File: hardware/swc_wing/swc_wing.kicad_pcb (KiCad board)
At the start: 2 copper layers, 62.8 x 58.7 mm, 51 parts, among them J1 Conn_01x06_Female, J2 Conn_01x04, J3 Conn_01x06_Female, J4 Conn_01x01_Female, Q1 2N7002, Q2 2N7002, Q3 2N7002, Q4 2N7002, Q5 2N7002, SW1 SW_Push_LED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

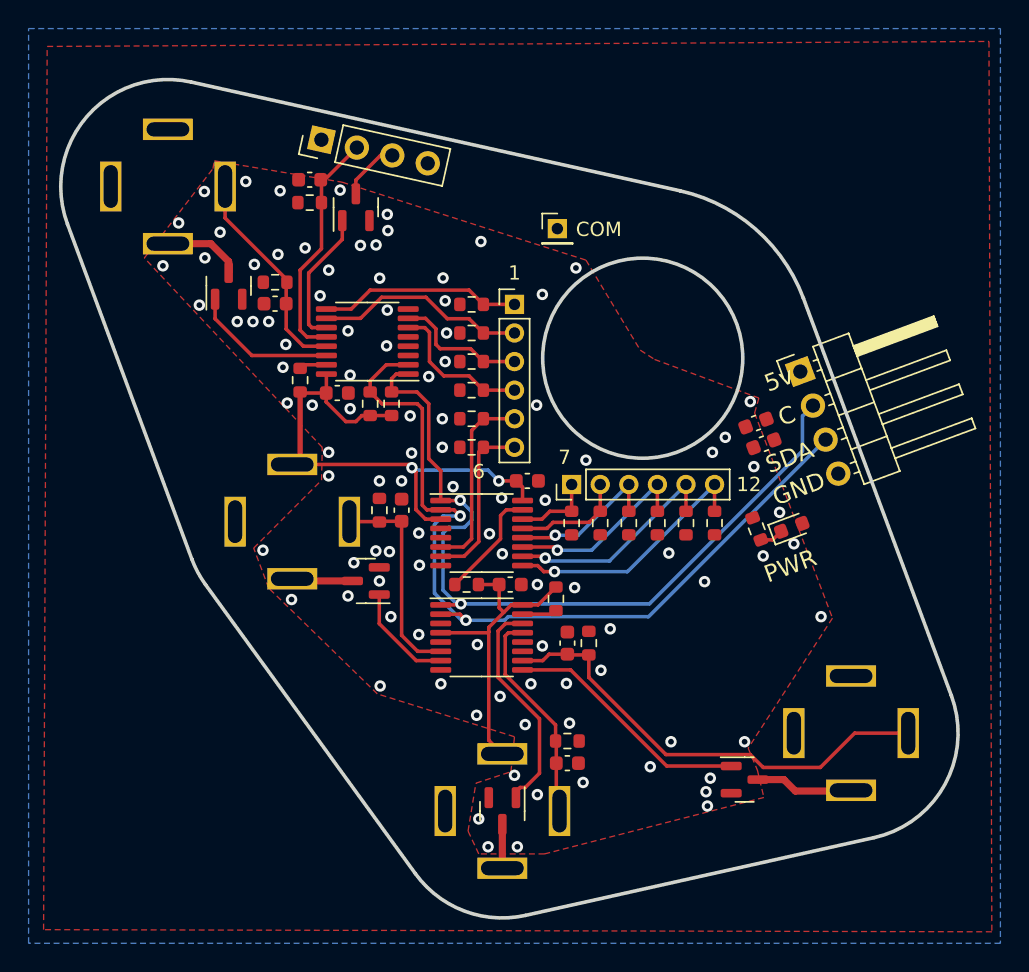
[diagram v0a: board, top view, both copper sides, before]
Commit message: 3.3v-ify wing
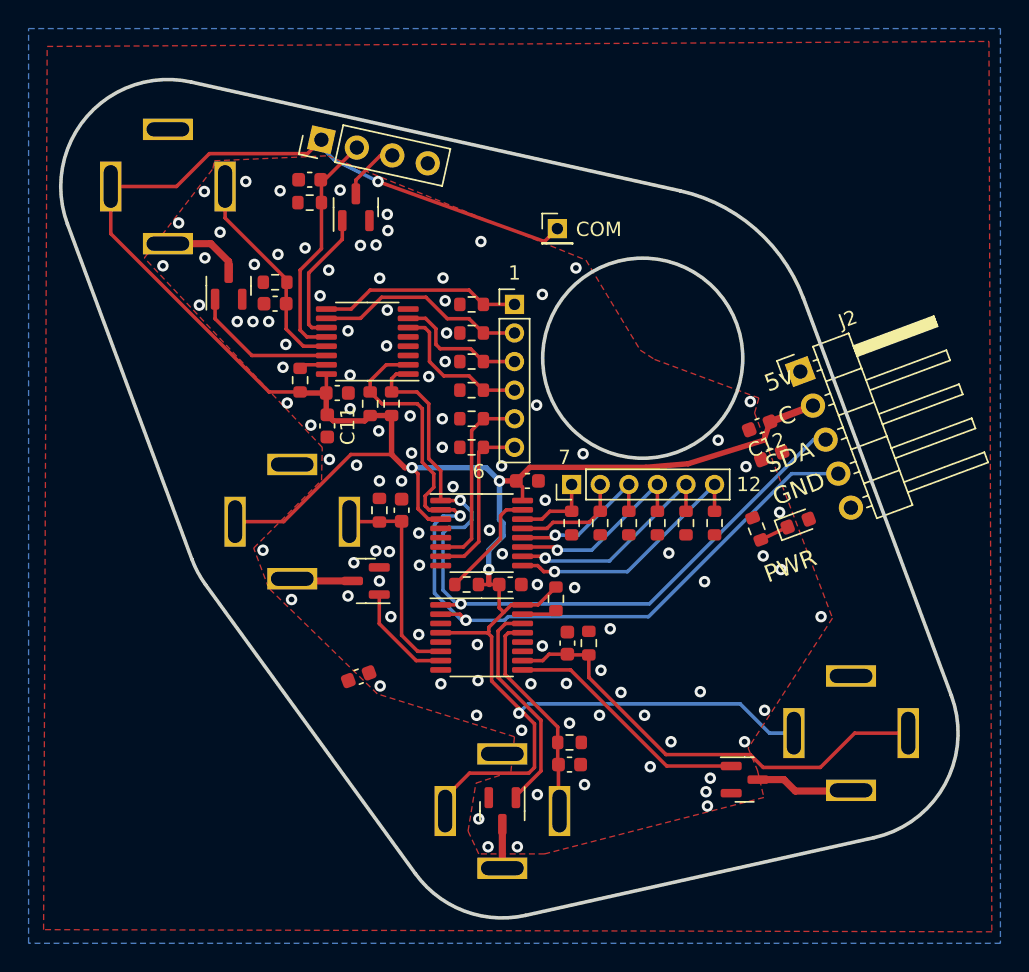
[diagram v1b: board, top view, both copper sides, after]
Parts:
- added C11: 1u, Capacitor_SMD:C_0603_1608Metric, F.Cu at (36.9, 83.8)
- added C12: 1u, Capacitor_SMD:C_0603_1608Metric, F.Cu at (67.2, 83.8)
- J2: value Conn_01x04 -> Conn_01x05; footprint Connector_PinHeader_2.54mm:PinHeader_1x04_P2.54mm_Horizontal -> Connector_PinHeader_2.54mm:PinHeader_1x05_P2.54mm_Horizontal
- moved C10 32.7 mm to (39.1, 101.3), turned to 20.4 degrees
- moved C9 2.55 mm to (68.0, 85.9)
- moved D1 0.54 mm to (69.8, 90.6)
- moved R4 0.18 mm to (53.9, 106.0)
- moved C4 0.18 mm to (53.9, 107.5)
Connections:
- C6 pad 1: +5V -> +3.3V
- C7 pad 1: +5V -> +3.3V
- C8 pad 1: +5V -> +3.3V
- J2 pad 2: SCL -> +3.3V
- J2 pad 3: SDA -> SCL
- J2 pad 4: GND -> SDA
- J4 pad 1: +5V -> +3.3V
- R10 pad 1: +5V -> +3.3V
- R6 pad 2: +5V -> +3.3V
- R7 pad 2: +5V -> +3.3V
- R8 pad 2: +5V -> +3.3V
- R9 pad 1: +5V -> +3.3V
- SW1 pad 1: +5V -> +3.3V
- SW2 pad 1: +5V -> +3.3V
- SW3 pad 1: +5V -> +3.3V
- SW4 pad 1: +5V -> +3.3V
- SW5 pad 1: +5V -> +3.3V
- U1 pad 16: +5V -> +3.3V
- U2 pad 16: +5V -> +3.3V
- U2 pad 3: +5V -> +3.3V
- U3 pad 16: +5V -> +3.3V
- U3 pad 4: +5V -> +3.3V
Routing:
- net +3.3V: track 0.00 -> 180.4 mm, vias 0 -> 5
- net +5V: track 59.2 -> 0.00 mm, vias 2 -> 0
- net SCL: track 56.7 -> 55.1 mm
- net GND: vias 101 -> 105

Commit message: wing tweaks
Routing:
- net GND: vias 105 -> 106
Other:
- board text added: "3v"
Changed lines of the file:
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@@
     (property "Sheetname" "")
     (attr through_hole)
-    (fp_text reference "J2" (at 4.385 -2.27 20.4) (layer "F.SilkS")
+    (fp_text reference "J2" (at 4.385 -2.27 20.4) (layer "F.SilkS") hide
       (effects (font (size 1 1) (thickness 0.15)))
     )
@@
     (property "Sheetname" "")
     (attr smd)
-    (fp_text reference "C11" (at 0 -1.43 90) (layer "F.SilkS")
+    (fp_text reference "C11" (at 0 -1.43 90) (layer "F.SilkS") hide
       (effects (font (size 1 1) (thickness 0.15)))
     )
@@
     (property "Sheetname" "")
     (attr smd)
-    (fp_text reference "C12" (at 0 -1.43 20.4) (layer "F.SilkS")
+    (fp_text reference "C12" (at 0 -1.43 20.4) (layer "F.SilkS") hide
       (effects (font (size 1 1) (thickness 0.15)))
     )
@@
   (gr_arc (start 50.770706 118.050213) (mid 46.48445 117.744753) (end 43.0694 115.136547) (layer "Edge.Cuts") (width 0.25))
   (gr_arc (start 28.380921 94.906654) (mid 27.838485 94.041203) (end 27.418667 93.110077) (layer "Edge.Cuts") (width 0.25))
-  (gr_text "SCL" (at 68.1 83.5 20.4) (layer "B.SilkS")
+  (gr_text "SCL" (at 68.9 85.9 20.4) (layer "B.SilkS")
     (effects (font (size 1.2 1.2) (thickness 0.15)) (justify mirror))
   )
@@
     (effects (font (size 1 1) (thickness 0.15)) (justify mirror))
   )
+  (gr_text "3v" (at 68.6 83.3 20.4) (layer "B.SilkS")
+    (effects (font (size 1.2 1.2) (thickness 0.15)) (justify mirror))
+  )
   (gr_text "7" (at 52.5 88) (layer "B.SilkS")
     (effects (font (size 1 1) (thickness 0.15)) (justify mirror))
@@
     (effects (font (size 1 1) (thickness 0.15)) (justify mirror))
   )
-  (gr_text "GND" (at 69.65 88.3 20.4) (layer "B.SilkS")
+  (gr_text "GND" (at 70.75 90.65 20.4) (layer "B.SilkS")
     (effects (font (size 1.2 1.2) (thickness 0.15)) (justify mirror))
   )
@@
     (effects (font (size 1.2 1.2) (thickness 0.15)) (justify mirror))
   )
-  (gr_text "SDA" (at 68.95 85.95 20.4) (layer "B.SilkS")
+  (gr_text "SDA" (at 69.75 88.25 20.4) (layer "B.SilkS")
     (effects (font (size 1.2 1.2) (thickness 0.15)) (justify mirror))
   )
@@
     (effects (font (size 1 1) (thickness 0.15)) (justify mirror))
   )
-  (gr_text "SDA" (at 69.25 86 20.4) (layer "F.SilkS")
+  (gr_text "SDA" (at 70.05 88.2 20.4) (layer "F.SilkS")
     (effects (font (size 1.2 1.2) (thickness 0.15)))
   )
@@
     (effects (font (size 1 1) (thickness 0.15)))
   )
-  (gr_text "GND" (at 69.9 88.2 20.4) (layer "F.SilkS")
+  (gr_text "GND" (at 72.75 91.8 20.4) (layer "F.SilkS")
     (effects (font (size 1.2 1.2) (thickness 0.15)))
   )
@@
     (effects (font (size 1 1) (thickness 0.15)))
   )
-  (gr_text "C" (at 69.05 83.1 20.4) (layer "F.SilkS")
+  (gr_text "C" (at 70.15 85.45 20.4) (layer "F.SilkS")
     (effects (font (size 1.2 1.2) (thickness 0.15)))
   )
-  (gr_text "PWR" (at 69.3 93.6 20.4) (layer "F.SilkS")
+  (gr_text "PWR" (at 68.8 93.7 20.4) (layer "F.SilkS")
     (effects (font (size 1.2 1.2) (thickness 0.15)))
   )
   (gr_text "7" (at 53.5 86) (layer "F.SilkS")
     (effects (font (size 1 1) (thickness 0.15)))
+  )
+  (gr_text "3v" (at 69.1 83.15 20.4) (layer "F.SilkS")
+    (effects (font (size 1.2 1.2) (thickness 0.15)))
   )
   (segment (start 36.494867 66.627287) (end 36.444867 66.577287) (width 0.25) (layer "F.Cu") (net 1))
@@
   (via (at 25.4 72.6) (size 0.8) (drill 0.4) (layers "F.Cu" "B.Cu") (net 2))
   (via (at 68.55 89.85) (size 0.8) (drill 0.4) (layers "F.Cu" "B.Cu") (net 2))
-  (via (at 56.7 98) (size 0.8) (drill 0.4) (layers "F.Cu" "B.Cu") (net 2))
+  (via (at 56.7 97.6) (size 0.8) (drill 0.4) (layers "F.Cu" "B.Cu") (net 2))
   (via (at 45.15 79.3) (size 0.8) (drill 0.4) (layers "F.Cu" "B.Cu") (net 2))
   (via (at 38.763148 93.374802) (size 0.8) (drill 0.4) (layers "F.Cu" "B.Cu") (net 2))
@@
   (via (at 39.220903 71.171965) (size 0.8) (drill 0.4) (layers "F.Cu" "B.Cu") (net 2))
   (via (at 33.8 79.7) (size 0.8) (drill 0.4) (layers "F.Cu" "B.Cu") (net 2))
-  (via (at 54.207826 95.114496) (size 0.8) (drill 0.4) (layers "F.Cu" "B.Cu") (net 2))
+  (via (at 54.25 95.2) (size 0.8) (drill 0.4) (layers "F.Cu" "B.Cu") (net 2))
   (via (at 54.9 108.9) (size 0.8) (drill 0.4) (layers "F.Cu" "B.Cu") (net 2))
   (via (at 47.35 104.05) (size 0.8) (drill 0.4) (layers "F.Cu" "B.Cu") (net 2))
@@
   (via (at 52.15 89) (size 0.8) (drill 0.4) (layers "F.Cu" "B.Cu") (net 2))
   (via (at 43.3 98.4) (size 0.8) (drill 0.4) (layers "F.Cu" "B.Cu") (net 2))
-  (via (at 63.3 94.7) (size 0.8) (drill 0.4) (layers "F.Cu" "B.Cu") (net 2))
+  (via (at 63.85 93.75) (size 0.8) (drill 0.4) (layers "F.Cu" "B.Cu") (net 2))
   (via (at 36.4 74.7) (size 0.8) (drill 0.4) (layers "F.Cu" "B.Cu") (net 2))
   (via (at 41.05 78.2) (size 0.8) (drill 0.4) (layers "F.Cu" "B.Cu") (net 2))
@@
   (via (at 42.7 83.1) (size 0.8) (drill 0.4) (layers "F.Cu" "B.Cu") (net 2))
   (via (at 51.6 94.9) (size 0.8) (drill 0.4) (layers "F.Cu" "B.Cu") (net 2))
-  (via (at 60.8 92.7) (size 0.8) (drill 0.4) (layers "F.Cu" "B.Cu") (net 2))
+  (via (at 61.5 92.7) (size 0.8) (drill 0.4) (layers "F.Cu" "B.Cu") (net 2))
   (via (at 41.140943 70.132385) (size 0.8) (drill 0.4) (layers "F.Cu" "B.Cu") (net 2))
   (via (at 45.25 77.3) (size 0.8) (drill 0.4) (layers "F.Cu" "B.Cu") (net 2))
@@
   (via (at 41.35 97.15) (size 0.8) (drill 0.4) (layers "F.Cu" "B.Cu") (net 2))
   (via (at 66.5 82.1) (size 0.8) (drill 0.4) (layers "F.Cu" "B.Cu") (net 2))
+  (via (at 59 95.35) (size 0.8) (drill 0.4) (layers "F.Cu" "B.Cu") (net 2))
   (via (at 38.35 77.15) (size 0.8) (drill 0.4) (layers "F.Cu" "B.Cu") (net 2))
   (via (at 51.95 99.2) (size 0.8) (drill 0.4) (layers "F.Cu" "B.Cu") (net 2))
@@
   (via (at 55.95 104.05) (size 0.8) (drill 0.4) (layers "F.Cu" "B.Cu") (net 2))
   (via (at 31.7 76.5) (size 0.8) (drill 0.4) (layers "F.Cu" "B.Cu") (net 2))
-  (via (at 68.65 93.85) (size 0.8) (drill 0.4) (layers "F.Cu" "B.Cu") (net 2))
+  (via (at 69.6 92.1) (size 0.8) (drill 0.4) (layers "F.Cu" "B.Cu") (net 2))
   (via (at 53.633963 101.823926) (size 0.8) (drill 0.4) (layers "F.Cu" "B.Cu") (net 2))
   (via (at 41.1 69) (size 0.8) (drill 0.4) (layers "F.Cu" "B.Cu") (net 2))
@@
   (via (at 46.2 90.1) (size 0.8) (drill 0.4) (layers "F.Cu" "B.Cu") (net 10))
   (segment (start 44.4 90.7) (end 44.4 95.5) (width 0.25) (layer "B.Cu") (net 10))
+  (segment (start 69.207911 87.142089) (end 72.656119 87.142089) (width 0.25) (layer "B.Cu") (net 10))
+  (segment (start 47.3 96.7) (end 59.65 96.7) (width 0.25) (layer "B.Cu") (net 10))
   (segment (start 46.2 90.1) (end 45 90.1) (width 0.25) (layer "B.Cu") (net 10))
   (segment (start 45 90.1) (end 44.4 90.7) (width 0.25) (layer "B.Cu") (net 10))
-  (segment (start 49.55 97.15) (end 49.3 97.4) (width 0.25) (layer "B.Cu") (net 10))
-  (segment (start 72.656119 87.142089) (end 69.39005 87.142089) (width 0.25) (layer "B.Cu") (net 10))
   (segment (start 44.4 95.5) (end 46.3 97.4) (width 0.25) (layer "B.Cu") (net 10))
-  (segment (start 59.382139 97.15) (end 49.55 97.15) (width 0.25) (layer "B.Cu") (net 10))
-  (segment (start 49.3 97.4) (end 46.6 97.4) (width 0.25) (layer "B.Cu") (net 10))
-  (segment (start 69.39005 87.142089) (end 59.382139 97.15) (width 0.25) (layer "B.Cu") (net 10))
+  (segment (start 46.6 97.4) (end 47.3 96.7) (width 0.25) (layer "B.Cu") (net 10))
   (segment (start 46.3 97.4) (end 46.6 97.4) (width 0.25) (layer "B.Cu") (net 10))
+  (segment (start 59.65 96.7) (end 69.207911 87.142089) (width 0.25) (layer "B.Cu") (net 10))
   (segment (start 35.825 76.925) (end 36.8375 76.925) (width 0.25) (layer "F.Cu") (net 11))
   (segment (start 37.95 70.75) (end 35.6 73.1) (width 0.25) (layer "F.Cu") (net 11))

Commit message: wing drc
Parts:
- moved R18 0.40 mm to (54.2, 91.0)
- moved R19 0.35 mm to (56.0, 91.0)
- moved R20 0.35 mm to (58.0, 91.0)
- moved R21 0.35 mm to (60.0, 91.0)
- moved R22 0.35 mm to (62.0, 91.0)
- moved R23 0.35 mm to (64.0, 91.0)
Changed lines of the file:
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@@
   (net 38 "Net-(Q1-Pad3)")
   (footprint "Resistor_SMD:R_0603_1608Metric" (layer "F.Cu")
-    (at 62 90.6 90)
+    (at 62 90.95 90)
     (descr "Resistor SMD 0603 (1608 Metric), square (rectangular) end terminal, IPC_7351 nominal, (Body size source: IPC-SM-782 page 72, https://www.pcb-3d.com/wordpress/wp-content/uploads/ipc-sm-782a_amendment_1_and_2.pdf), generated with kicad-footprint-generator")
     (tags "resistor")
@@
   )
   (footprint "Resistor_SMD:R_0603_1608Metric" (layer "F.Cu")
-    (at 58 90.6 90)
+    (at 58 90.95 90)
     (descr "Resistor SMD 0603 (1608 Metric), square (rectangular) end terminal, IPC_7351 nominal, (Body size source: IPC-SM-782 page 72, https://www.pcb-3d.com/wordpress/wp-content/uploads/ipc-sm-782a_amendment_1_and_2.pdf), generated with kicad-footprint-generator")
     (tags "resistor")
@@
   )
   (footprint "Resistor_SMD:R_0603_1608Metric" (layer "F.Cu")
-    (at 54 90.6 90)
+    (at 54.2 90.95 90)
     (descr "Resistor SMD 0603 (1608 Metric), square (rectangular) end terminal, IPC_7351 nominal, (Body size source: IPC-SM-782 page 72, https://www.pcb-3d.com/wordpress/wp-content/uploads/ipc-sm-782a_amendment_1_and_2.pdf), generated with kicad-footprint-generator")
     (tags "resistor")
@@
   )
   (footprint "Resistor_SMD:R_0603_1608Metric" (layer "F.Cu")
-    (at 60 90.6 90)
+    (at 60 90.95 90)
     (descr "Resistor SMD 0603 (1608 Metric), square (rectangular) end terminal, IPC_7351 nominal, (Body size source: IPC-SM-782 page 72, https://www.pcb-3d.com/wordpress/wp-content/uploads/ipc-sm-782a_amendment_1_and_2.pdf), generated with kicad-footprint-generator")
     (tags "resistor")
@@
   )
   (footprint "Resistor_SMD:R_0603_1608Metric" (layer "F.Cu")
-    (at 56 90.6 90)
+    (at 56 90.95 90)
     (descr "Resistor SMD 0603 (1608 Metric), square (rectangular) end terminal, IPC_7351 nominal, (Body size source: IPC-SM-782 page 72, https://www.pcb-3d.com/wordpress/wp-content/uploads/ipc-sm-782a_amendment_1_and_2.pdf), generated with kicad-footprint-generator")
     (tags "resistor")
@@
   )
   (footprint "Resistor_SMD:R_0603_1608Metric" (layer "F.Cu")
-    (at 64 90.6 90)
+    (at 64 90.95 90)
     (descr "Resistor SMD 0603 (1608 Metric), square (rectangular) end terminal, IPC_7351 nominal, (Body size source: IPC-SM-782 page 72, https://www.pcb-3d.com/wordpress/wp-content/uploads/ipc-sm-782a_amendment_1_and_2.pdf), generated with kicad-footprint-generator")
     (tags "resistor")
@@
   (via (at 42.7 83.1) (size 0.8) (drill 0.4) (layers "F.Cu" "B.Cu") (net 2))
   (via (at 51.6 94.9) (size 0.8) (drill 0.4) (layers "F.Cu" "B.Cu") (net 2))
-  (via (at 61.5 92.7) (size 0.8) (drill 0.4) (layers "F.Cu" "B.Cu") (net 2))
+  (via (at 61.4 93) (size 0.8) (drill 0.4) (layers "F.Cu" "B.Cu") (net 2))
   (via (at 41.140943 70.132385) (size 0.8) (drill 0.4) (layers "F.Cu" "B.Cu") (net 2))
   (via (at 45.25 77.3) (size 0.8) (drill 0.4) (layers "F.Cu" "B.Cu") (net 2))
@@
   (via (at 42.825 86.725) (size 0.8) (drill 0.4) (layers "F.Cu" "B.Cu") (net 12))
   (segment (start 65.8 103.25) (end 67.85 105.3) (width 0.25) (layer "B.Cu") (net 12))
-  (segment (start 43 86.9) (end 42.825 86.725) (width 0.25) (layer "B.Cu") (net 12))
   (segment (start 36.490075 64.290075) (end 36.490075 63.77753) (width 0.25) (layer "B.Cu") (net 12))
   (segment (start 48.95 90.35) (end 48.95 87.65) (width 0.38) (layer "B.Cu") (net 12))
@@
   (segment (start 51.625 93.575) (end 51.8 93.75) (width 0.25) (layer "F.Cu") (net 32))
   (segment (start 50.5625 93.575) (end 51.625 93.575) (width 0.25) (layer "F.Cu") (net 32))
-  (segment (start 64 89.775) (end 64 87.9) (width 0.25) (layer "F.Cu") (net 32))
   (segment (start 52.05 94) (end 52.8 94) (width 0.25) (layer "F.Cu") (net 32))
   (segment (start 51.8 93.75) (end 52.05 94) (width 0.25) (layer "F.Cu") (net 32))
+  (segment (start 64 87.9) (end 64 90.125) (width 0.25) (layer "F.Cu") (net 32))
   (via (at 52.8 94) (size 0.8) (drill 0.4) (layers "F.Cu" "B.Cu") (net 32))
   (segment (start 52.8 94) (end 57.9 94) (width 0.25) (layer "B.Cu") (net 32))
   (segment (start 57.9 94) (end 64 87.9) (width 0.25) (layer "B.Cu") (net 32))
-  (segment (start 62 87.9) (end 62 89.775) (width 0.25) (layer "F.Cu") (net 33))
   (segment (start 50.5625 92.925) (end 52.025 92.925) (width 0.25) (layer "F.Cu") (net 33))
   (segment (start 52.025 92.925) (end 52.15 93.05) (width 0.25) (layer "F.Cu") (net 33))
+  (segment (start 62 87.9) (end 62 90.125) (width 0.25) (layer "F.Cu") (net 33))
   (via (at 52.15 93.05) (size 0.8) (drill 0.4) (layers "F.Cu" "B.Cu") (net 33))
   (segment (start 56.65 93.25) (end 62 87.9) (width 0.25) (layer "B.Cu") (net 33))
@@
   (segment (start 50.5625 92.275) (end 52.775 92.275) (width 0.25) (layer "F.Cu") (net 34))
   (segment (start 52.775 92.275) (end 53 92.5) (width 0.25) (layer "F.Cu") (net 34))
-  (segment (start 60 87.9) (end 60 89.775) (width 0.25) (layer "F.Cu") (net 34))
+  (segment (start 60 87.9) (end 60 90.125) (width 0.25) (layer "F.Cu") (net 34))
   (via (at 53 92.5) (size 0.8) (drill 0.4) (layers "F.Cu" "B.Cu") (net 34))
   (segment (start 55.4 92.5) (end 60 87.9) (width 0.25) (layer "B.Cu") (net 34))
   (segment (start 53 92.5) (end 55.4 92.5) (width 0.25) (layer "B.Cu") (net 34))
-  (segment (start 58 87.9) (end 58 89.775) (width 0.25) (layer "F.Cu") (net 35))
+  (segment (start 58 87.9) (end 58 90.125) (width 0.25) (layer "F.Cu") (net 35))
   (segment (start 50.5625 91.625) (end 52.675 91.625) (width 0.25) (layer "F.Cu") (net 35))
   (segment (start 52.675 91.625) (end 52.85 91.45) (width 0.25) (layer "F.Cu") (net 35))
@@
   (segment (start 54.45 91.45) (end 58 87.9) (width 0.25) (layer "B.Cu") (net 35))
   (segment (start 52.85 91.45) (end 54.45 91.45) (width 0.25) (layer "B.Cu") (net 35))
-  (segment (start 52.7 90.55) (end 52.275 90.975) (width 0.25) (layer "F.Cu") (net 36))
-  (segment (start 56 89.775) (end 55.225 90.55) (width 0.25) (layer "F.Cu") (net 36))
-  (segment (start 55.225 90.55) (end 52.7 90.55) (width 0.25) (layer "F.Cu") (net 36))
-  (segment (start 56 89.775) (end 56 87.9) (width 0.25) (layer "F.Cu") (net 36))
-  (segment (start 52.275 90.975) (end 50.5625 90.975) (width 0.25) (layer "F.Cu") (net 36))
-  (segment (start 54 87.9) (end 54 89.775) (width 0.25) (layer "F.Cu") (net 37))
-  (segment (start 50.5625 90.325) (end 51.925 90.325) (width 0.25) (layer "F.Cu") (net 37))
-  (segment (start 52.475 89.775) (end 54 89.775) (width 0.25) (layer "F.Cu") (net 37))
-  (segment (start 51.925 90.325) (end 52.475 89.775) (width 0.25) (layer "F.Cu") (net 37))
+  (segment (start 52.4 90.7) (end 53.4 90.7) (width 0.25) (layer "F.Cu") (net 36))
+  (segment (start 53.65 90.95) (end 55.175 90.95) (width 0.25) (layer "F.Cu") (net 36))
+  (segment (start 55.175 90.95) (end 56 90.125) (width 0.25) (layer "F.Cu") (net 36))
+  (segment (start 50.5625 90.975) (end 52.125 90.975) (width 0.25) (layer "F.Cu") (net 36))
+  (segment (start 53.4 90.7) (end 53.65 90.95) (width 0.25) (layer "F.Cu") (net 36))
+  (segment (start 56 90.125) (end 56 87.9) (width 0.25) (layer "F.Cu") (net 36))
+  (segment (start 52.125 90.975) (end 52.4 90.7) (width 0.25) (layer "F.Cu") (net 36))
+  (segment (start 54 87.9) (end 54 89.925) (width 0.25) (layer "F.Cu") (net 37))
+  (segment (start 52.175 90.125) (end 51.975 90.325) (width 0.25) (layer "F.Cu") (net 37))
+  (segment (start 54 89.925) (end 54.2 90.125) (width 0.25) (layer "F.Cu") (net 37))
+  (segment (start 51.975 90.325) (end 50.5625 90.325) (width 0.25) (layer "F.Cu") (net 37))
+  (segment (start 54.2 90.125) (end 52.175 90.125) (width 0.25) (layer "F.Cu") (net 37))
   (segment (start 38.9 67.5625) (end 38.9 66.6) (width 0.25) (layer "F.Cu") (net 38))
   (segment (start 40.622957 64.877043) (end 41.449659 64.877043) (width 0.25) (layer "F.Cu") (net 38))
